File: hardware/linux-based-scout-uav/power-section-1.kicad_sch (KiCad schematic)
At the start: 0 parts

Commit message: Schematic update
Work done on the USB-C receptacle and power delivery section.
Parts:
- added C4: 1uF, symbol Device:C
- added C5, C6: 0.1uF, symbol Device:C
- added J5: GSB1C41110SSHR, GSB1C41110SSHR:AMPHENOL_GSB1C41110SSHR, symbol GSB1C41110SSHR:GSB1C41110SSHR
- added Q1, Q2: DMP3013SFV, Package_SON:Diodes_PowerDI3333-8, symbol Transistor_FET:DMP3013SFV
- added R18, R19, R20, R21: DNP, symbol Device:R
- added U9: CYPD3177-24LQ, Package_DFN_QFN:QFN-24-1EP_4x4mm_P0.5mm_EP2.75x2.75mm, symbol Interface_USB:CYPD3177-24LQ
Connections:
- new net: U9.19 (GND), U9.22 (GND), U9.25 (GND)
- new net: Q1.1 (S), Q1.2 (S), Q1.3 (S)
- new net: Q2.1 (S), Q2.2 (S), Q2.3 (S)
- new net  CC1: U9.15 (CC1)
- new net +VBUS: J5.A4_B9 (VBUS_A), J5.B4_A9 (VBUS_B), U9.18 (VBUS_IN)
- new net +VDDIO_3V3: C4.1, C5.1, C6.1, R18.1, R20.1, U9.23 (VDDD)
- new net CC1: J5.A5 (CC1)
- new net CC2: J5.B5 (CC2), U9.14 (CC2)
- new net GND: C4.2, C5.2, C6.2, J5.A1_B12 (GND_A), J5.B1_A12 (GND_B), J5.SH1 (SHIELD), J5.SH2 (SHIELD), J5.SH3 (SHIELD), J5.SH4 (SHIELD), R19.2, R21.2
- new net VBUS_MAX: R18.2, R19.1, U9.2 (VBUS_MAX)
- new net VBUS_MIN: R20.2, R21.1, U9.1 (VBUS_MIN)

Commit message: Schematic update USB DP section
USB DP section updated, voltage and current setting resistor divider.
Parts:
- added R22, R23, R24, R25: DNP, symbol Device:R
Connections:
- net +VDDIO_3V3: now also R22.1, R24.1
- net GND: now also R23.2, R25.2
- net ISNK_COARSE: now reaches U9.5 (ISNK_COARSE)
- net ISNK_COARSE: now also R22.2, R23.1
- net ISNK_FINE: now reaches U9.6 (ISNK_FINE)
- net ISNK_FINE: now also R24.2, R25.1
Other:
- note added: "CC1/CC2 pull-up/down resistor network CC1/CC2プルアップ/ダウン抵抗ネットワーク"
- note added: "Resistor divider to set the operating current requested from the power adapter 電源アダプタから要求される動作電流を設定するための抵抗分圧器"
- moved on the sheet: Q1, Q2

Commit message: schematic update
schematic update
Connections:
- net GND: now also U9.19 (GND), U9.22 (GND), U9.25 (GND)
- net USB_DP1: now reaches J5.A6 (DP1)
- net USB_DM1: now reaches J5.A7 (DN1)
- net USB_DP2: now reaches J5.B6 (DP2)
- net USB_DM2: now reaches J5.B7 (DN2)
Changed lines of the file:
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@@
+	(wire
+		(pts
+			(xy 36.83 73.66) (xy 55.88 73.66)
+		)
+		(stroke
+			(width 0)
+			(type default)
+		)
+	)
 	(wire
 		(pts
@@
 	(wire
 		(pts
+			(xy 187.96 97.79) (xy 187.96 104.14)
+		)
+		(stroke
+			(width 0)
+			(type default)
+		)
+	)
+	(wire
+		(pts
 			(xy 60.96 163.83) (xy 73.66 163.83)
 		)
@@
 	(wire
 		(pts
+			(xy 91.44 73.66) (xy 114.3 73.66)
+		)
+		(stroke
+			(width 0)
+			(type default)
+		)
+	)
+	(wire
+		(pts
 			(xy 130.81 163.83) (xy 143.51 163.83)
 		)
@@
 	(wire
 		(pts
+			(xy 36.83 76.2) (xy 55.88 76.2)
+		)
+		(stroke
+			(width 0)
+			(type default)
+		)
+	)
+	(wire
+		(pts
 			(xy 55.88 66.04) (xy 46.99 66.04)
 		)
@@
 		(pts
 			(xy 73.66 176.53) (xy 73.66 185.42)
+		)
+		(stroke
+			(width 0)
+			(type default)
+		)
+	)
+	(wire
+		(pts
+			(xy 91.44 76.2) (xy 114.3 76.2)
 		)
 		(stroke
@@
 			)
 			(justify left bottom)
+		)
+	)
+	(global_label "USB_DM1"
+		(shape bidirectional)
+		(at 36.83 76.2 180)
+		(fields_autoplaced yes)
+		(effects
+			(font
+				(size 1.27 1.27)
+			)
+			(justify right)
+		)
+		(property "Intersheetrefs" "${INTERSHEET_REFS}"
+			(at 24.025 76.2 0)
+			(effects
+				(font
+					(size 1.27 1.27)
+				)
+				(justify right)
+				(hide yes)
+			)
+		)
+	)
+	(global_label "USB_DP1"
+		(shape bidirectional)
+		(at 36.83 73.66 180)
+		(fields_autoplaced yes)
+		(effects
+			(font
+				(size 1.27 1.27)
+			)
+			(justify right)
+		)
+		(property "Intersheetrefs" "${INTERSHEET_REFS}"
+			(at 24.2064 73.66 0)
+			(effects
+				(font
+					(size 1.27 1.27)
+				)
+				(justify right)
+				(hide yes)
+			)
+		)
+	)
+	(global_label "USB_DP2"
+		(shape bidirectional)
+		(at 114.3 76.2 0)
+		(fields_autoplaced yes)
+		(effects
+			(font
+				(size 1.27 1.27)
+			)
+			(justify left)
+		)
+		(property "Intersheetrefs" "${INTERSHEET_REFS}"
+			(at 126.9236 76.2 0)
+			(effects
+				(font
+					(size 1.27 1.27)
+				)
+				(justify left)
+				(hide yes)
+			)
+		)
+	)
+	(global_label "USB_DM2"
+		(shape bidirectional)
+		(at 114.3 73.66 0)
+		(fields_autoplaced yes)
+		(effects
+			(font
+				(size 1.27 1.27)
+			)
+			(justify left)
+		)
+		(property "Intersheetrefs" "${INTERSHEET_REFS}"
+			(at 127.105 73.66 0)
+			(effects
+				(font
+					(size 1.27 1.27)
+				)
+				(justify left)
+				(hide yes)
+			)
 		)
 	)
@@
 					(unit 1)
 				)
+			)
+		)
+	)
+	(symbol
+		(lib_id "power:GND")
+		(at 187.96 104.14 0)
+		(unit 1)
+		(exclude_from_sim no)
+		(in_bom yes)
+		(on_board yes)
+		(dnp no)
+		(fields_autoplaced yes)
+		(property "Reference" "#PWR040"
+			(at 187.96 110.49 0)
+			(effects
+				(font
+					(size 1.27 1.27)
+				)
+				(hide yes)
+			)
+		)
+		(property "Value" "GND"
+			(at 187.96 109.22 0)
+			(effects
+				(font
+					(size 1.27 1.27)
+				)
+			)
+		)
+		(property "Footprint" ""
+			(at 187.96 104.14 0)
+			(effects
+				(font
+					(size 1.27 1.27)
+				)
+				(hide yes)
+			)
+		)
+		(property "Datasheet" ""
+			(at 187.96 104.14 0)
+			(effects
+				(font
+					(size 1.27 1.27)
+				)
+				(hide yes)
+			)
+		)
+		(property "Description" "Power symbol creates a global label with name \"GND\" , ground"
+			(at 187.96 104.14 0)
+			(effects
+				(font
+					(size 1.27 1.27)
+				)
+				(hide yes)
+			)
+		)
+		(pin "1"
+		)
+		(instances
+			(project "linux-based-scout-uav"
+				(path "/e9b29a7c-bbe5-4ab4-acee-985586e1266a/a91084ce-30c2-4c08-a9de-234ec8328b30"
+					(reference "#PWR040")
+					(unit 1)
+				)

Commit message: Schematic and board update
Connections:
- net USB_DM1 renamed USB_DM
- net USB_DM2: no longer names the net of J5.B7 (DN2)
- net USB_DP1 renamed USB_DP
- net USB_DP2: no longer names the net of J5.B6 (DP2)
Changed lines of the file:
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@@
-	(wire
-		(pts
-			(xy 91.44 73.66) (xy 114.3 73.66)
-		)
-		(stroke
-			(width 0)
-			(type default)
-		)
-	)
 	(wire
 		(pts
@@
 		(pts
 			(xy 73.66 176.53) (xy 73.66 185.42)
-		)
-		(stroke
-			(width 0)
-			(type default)
-		)
-	)
-	(wire
-		(pts
-			(xy 91.44 76.2) (xy 114.3 76.2)
 		)
 		(stroke
@@
 		)
 	)
-	(global_label "USB_DM1"
+	(global_label "USB_DM"
 		(shape bidirectional)
 		(at 36.83 76.2 180)
@@
 		)
 		(property "Intersheetrefs" "${INTERSHEET_REFS}"
-			(at 24.025 76.2 0)
+			(at 25.2345 76.2 0)
 			(effects
 				(font
@@
 		)
 	)
-	(global_label "USB_DP1"
+	(global_label "USB_DP"
 		(shape bidirectional)
 		(at 36.83 73.66 180)
@@
 		)
 		(property "Intersheetrefs" "${INTERSHEET_REFS}"
-			(at 24.2064 73.66 0)
+			(at 25.4159 73.66 0)
 			(effects
 				(font
@@
 				(hide yes)
 			)
-		)
-	)
-	(global_label "USB_DP2"
-		(shape bidirectional)
-		(at 114.3 76.2 0)
-		(fields_autoplaced yes)
-		(effects
-			(font
-				(size 1.27 1.27)
-			)
-			(justify left)
-		)
-		(property "Intersheetrefs" "${INTERSHEET_REFS}"
-			(at 126.9236 76.2 0)
-			(effects
-				(font
-					(size 1.27 1.27)
-				)
-				(justify left)
-				(hide yes)
-			)
-		)
-	)
-	(global_label "USB_DM2"
-		(shape bidirectional)
-		(at 114.3 73.66 0)
-		(fields_autoplaced yes)
-		(effects
-			(font
-				(size 1.27 1.27)
-			)
-			(justify left)
-		)
-		(property "Intersheetrefs" "${INTERSHEET_REFS}"
-			(at 127.105 73.66 0)
-			(effects
-				(font
-					(size 1.27 1.27)
-				)
-				(justify left)
-				(hide yes)
-			)

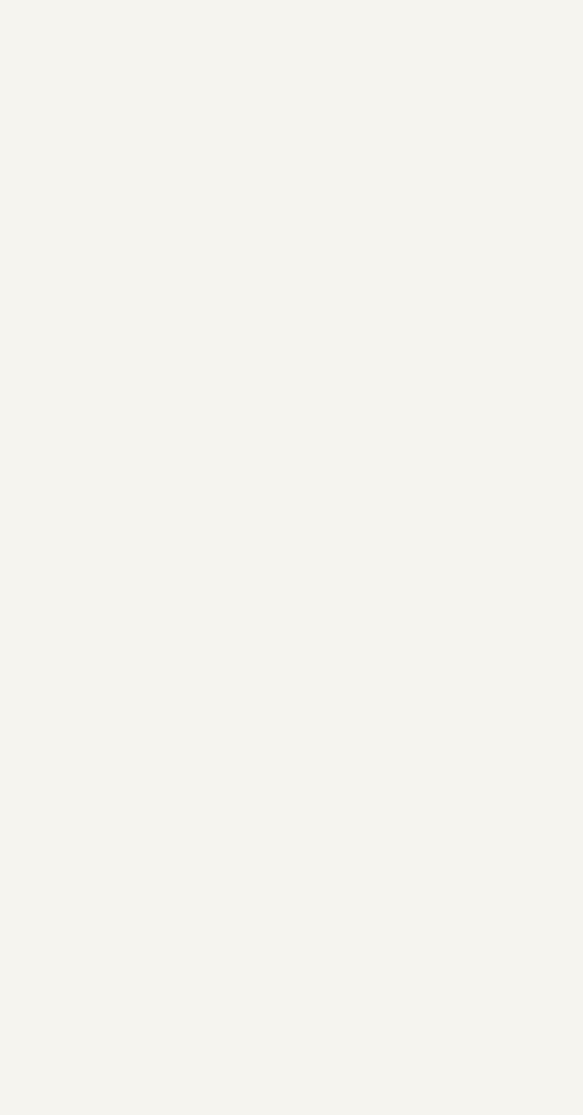
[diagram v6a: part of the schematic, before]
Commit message: Added TPS65217C PMIC
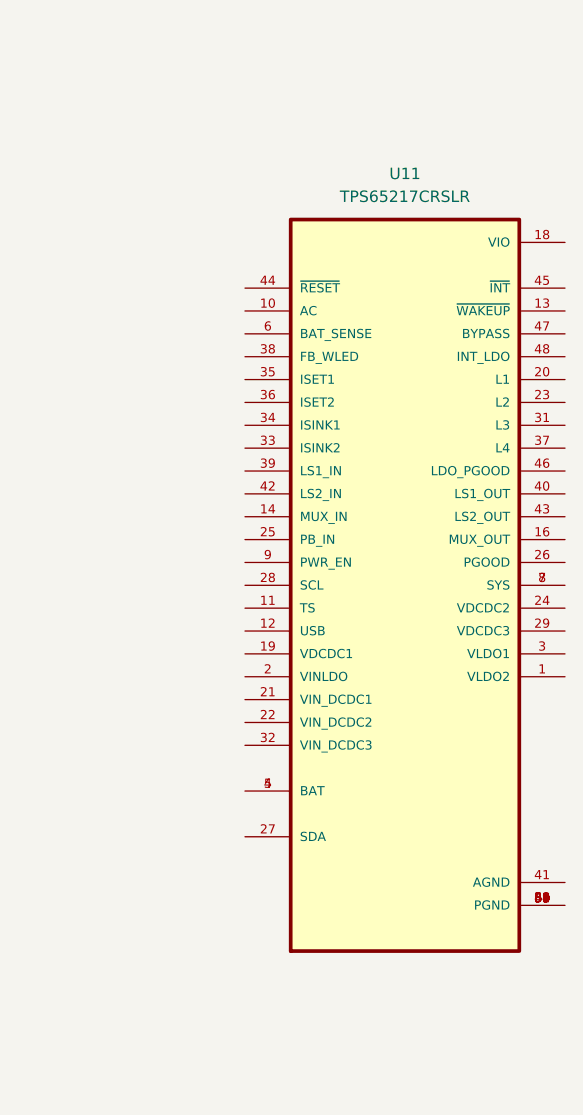
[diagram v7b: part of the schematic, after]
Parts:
- added U11: TPS65217CRSLR, TPS65217CRSLR:IC_TPS65217CRSLR, symbol TPS65217CRSLR:TPS65217CRSLR
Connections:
- new net: U11.30 (PGND), U11.49 (PGND), U11.50 (PGND), U11.51 (PGND), U11.52 (PGND), U11.53 (PGND), U11.54 (PGND), U11.55 (PGND), U11.56 (PGND), U11.57 (PGND), U11.58 (PGND), U11.59 (PGND), U11.60 (PGND), U11.61 (PGND), U11.62 (PGND), U11.63 (PGND), U11.64 (PGND), U11.65 (PGND)
- new net: U11.4 (BAT), U11.5 (BAT)
- new net: U11.7 (SYS), U11.8 (SYS)

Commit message: Update
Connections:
- net GND: now also U11.30 (PGND), U11.41 (AGND), U11.49 (PGND), U11.50 (PGND), U11.51 (PGND), U11.52 (PGND), U11.53 (PGND), U11.54 (PGND), U11.55 (PGND), U11.56 (PGND), U11.57 (PGND), U11.58 (PGND), U11.59 (PGND), U11.60 (PGND), U11.61 (PGND), U11.62 (PGND), U11.63 (PGND), U11.64 (PGND), U11.65 (PGND)
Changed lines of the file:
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@@
+	)
+	(junction
+		(at 331.47 163.83)
+		(diameter 0)
+		(color 0 0 0 0)
 	)
 	(junction
@@
 	(wire
 		(pts
+			(xy 331.47 161.29) (xy 331.47 163.83)
+		)
+		(stroke
+			(width 0)
+			(type default)
+		)
+	)
+	(wire
+		(pts
 			(xy 50.8 163.83) (xy 50.8 168.91)
 		)
@@
 	(wire
 		(pts
+			(xy 331.47 163.83) (xy 331.47 172.72)
+		)
+		(stroke
+			(width 0)
+			(type default)
+		)
+	)
+	(wire
+		(pts
 			(xy 36.83 76.2) (xy 55.88 76.2)
 		)
@@
 	(wire
 		(pts
+			(xy 322.58 163.83) (xy 331.47 163.83)
+		)
+		(stroke
+			(width 0)
+			(type default)
+		)
+	)
+	(wire
+		(pts
 			(xy 38.1 163.83) (xy 50.8 163.83)
 		)
@@
 		(pts
 			(xy 147.32 64.77) (xy 170.18 64.77)
+		)
+		(stroke
+			(width 0)
+			(type default)
+		)
+	)
+	(wire
+		(pts
+			(xy 322.58 161.29) (xy 331.47 161.29)
 		)
 		(stroke
@@
 					(unit 1)
 				)
+			)
+		)
+	)
+	(symbol
+		(lib_id "power:GND")
+		(at 331.47 172.72 0)
+		(unit 1)
+		(exclude_from_sim no)
+		(in_bom yes)
+		(on_board yes)
+		(dnp no)
+		(fields_autoplaced yes)
+		(property "Reference" "#PWR045"
+			(at 331.47 179.07 0)
+			(effects
+				(font
+					(size 1.27 1.27)
+				)
+				(hide yes)
+			)
+		)
+		(property "Value" "GND"
+			(at 331.47 177.8 0)
+			(effects
+				(font
+					(size 1.27 1.27)
+				)
+			)
+		)
+		(property "Footprint" ""
+			(at 331.47 172.72 0)
+			(effects
+				(font
+					(size 1.27 1.27)
+				)
+				(hide yes)
+			)
+		)
+		(property "Datasheet" ""
+			(at 331.47 172.72 0)
+			(effects
+				(font
+					(size 1.27 1.27)
+				)
+				(hide yes)
+			)
+		)
+		(property "Description" "Power symbol creates a global label with name \"GND\" , ground"
+			(at 331.47 172.72 0)
+			(effects
+				(font
+					(size 1.27 1.27)
+				)
+				(hide yes)
+			)
+		)
+		(pin "1"
+		)
+		(instances
+			(project "linux-based-scout-uav"
+				(path "/e9b29a7c-bbe5-4ab4-acee-985586e1266a/a91084ce-30c2-4c08-a9de-234ec8328b30"
+					(reference "#PWR045")
+					(unit 1)
+				)
